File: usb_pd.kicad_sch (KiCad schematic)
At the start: 69 parts

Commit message: added digi-pote symbol, added USB_source voltage regulators
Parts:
- U?: symbol smarthome:TPS5403DR -> airsoft_controller:TPS5403DR
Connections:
- net +3V3: no longer C?.2, L?.2, U?.5 (VSENSE)
- new net +3.3V: C?.2, L?.2, U?.5 (VSENSE)
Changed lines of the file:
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@@
   (symbol (lib_id "power:GND") (at 233.68 72.39 0) (mirror y) (unit 1)
     (in_bom yes) (on_board yes) (fields_autoplaced)
-    (property "Reference" "#PWR?" (id 0) (at 233.68 78.74 0)
+    (property "Reference" "#PWR0129" (id 0) (at 233.68 78.74 0)
       (effects (font (size 1.27 1.27)) hide)
     )
@@
   (symbol (lib_id "power:GND") (at 57.15 173.99 0) (unit 1)
     (in_bom yes) (on_board yes) (fields_autoplaced)
-    (property "Reference" "#PWR?" (id 0) (at 57.15 180.34 0)
+    (property "Reference" "#PWR0147" (id 0) (at 57.15 180.34 0)
       (effects (font (size 1.27 1.27)) hide)
     )
@@
   (symbol (lib_id "power:GND") (at 96.52 106.68 0) (unit 1)
     (in_bom yes) (on_board yes) (fields_autoplaced)
-    (property "Reference" "#PWR?" (id 0) (at 96.52 113.03 0)
+    (property "Reference" "#PWR0135" (id 0) (at 96.52 113.03 0)
       (effects (font (size 1.27 1.27)) hide)
     )
@@
   (symbol (lib_id "power:GND") (at 120.65 57.15 0) (unit 1)
     (in_bom yes) (on_board yes) (fields_autoplaced)
-    (property "Reference" "#PWR?" (id 0) (at 120.65 63.5 0)
+    (property "Reference" "#PWR0137" (id 0) (at 120.65 63.5 0)
       (effects (font (size 1.27 1.27)) hide)
     )
@@
   (symbol (lib_id "power:GND") (at 168.91 128.27 0) (unit 1)
     (in_bom yes) (on_board yes) (fields_autoplaced)
-    (property "Reference" "#PWR?" (id 0) (at 168.91 134.62 0)
+    (property "Reference" "#PWR0124" (id 0) (at 168.91 134.62 0)
       (effects (font (size 1.27 1.27)) hide)
     )
@@
   (symbol (lib_id "power:+3.3V") (at 104.14 160.02 0) (unit 1)
     (in_bom yes) (on_board yes) (fields_autoplaced)
-    (property "Reference" "#PWR?" (id 0) (at 104.14 163.83 0)
+    (property "Reference" "#PWR0150" (id 0) (at 104.14 163.83 0)
       (effects (font (size 1.27 1.27)) hide)
     )
@@
   (symbol (lib_id "power:GND") (at 262.89 133.35 0) (unit 1)
     (in_bom yes) (on_board yes) (fields_autoplaced)
-    (property "Reference" "#PWR?" (id 0) (at 262.89 139.7 0)
+    (property "Reference" "#PWR0122" (id 0) (at 262.89 139.7 0)
       (effects (font (size 1.27 1.27)) hide)
     )
@@
   (symbol (lib_id "power:GND") (at 74.93 173.99 0) (unit 1)
     (in_bom yes) (on_board yes) (fields_autoplaced)
-    (property "Reference" "#PWR?" (id 0) (at 74.93 180.34 0)
+    (property "Reference" "#PWR0142" (id 0) (at 74.93 180.34 0)
       (effects (font (size 1.27 1.27)) hide)
     )
@@
   (symbol (lib_id "power:GND") (at 138.43 115.57 0) (unit 1)
     (in_bom yes) (on_board yes) (fields_autoplaced)
-    (property "Reference" "#PWR?" (id 0) (at 138.43 121.92 0)
+    (property "Reference" "#PWR0125" (id 0) (at 138.43 121.92 0)
       (effects (font (size 1.27 1.27)) hide)
     )
@@
   (symbol (lib_id "power:GND") (at 62.23 96.52 0) (unit 1)
     (in_bom yes) (on_board yes) (fields_autoplaced)
-    (property "Reference" "#PWR?" (id 0) (at 62.23 102.87 0)
+    (property "Reference" "#PWR0134" (id 0) (at 62.23 102.87 0)
       (effects (font (size 1.27 1.27)) hide)
     )
@@
   (symbol (lib_id "power:GND") (at 88.9 106.68 0) (unit 1)
     (in_bom yes) (on_board yes) (fields_autoplaced)
-    (property "Reference" "#PWR?" (id 0) (at 88.9 113.03 0)
+    (property "Reference" "#PWR0136" (id 0) (at 88.9 113.03 0)
       (effects (font (size 1.27 1.27)) hide)
     )
@@
   (symbol (lib_id "power:GND") (at 201.93 109.22 0) (unit 1)
     (in_bom yes) (on_board yes) (fields_autoplaced)
-    (property "Reference" "#PWR?" (id 0) (at 201.93 115.57 0)
+    (property "Reference" "#PWR0130" (id 0) (at 201.93 115.57 0)
       (effects (font (size 1.27 1.27)) hide)
     )
@@
   (symbol (lib_id "power:VBUS") (at 138.43 62.23 0) (unit 1)
     (in_bom yes) (on_board yes) (fields_autoplaced)
-    (property "Reference" "#PWR?" (id 0) (at 138.43 66.04 0)
+    (property "Reference" "#PWR0121" (id 0) (at 138.43 66.04 0)
       (effects (font (size 1.27 1.27)) hide)
     )
@@
   (symbol (lib_id "power:GND") (at 67.31 173.99 0) (unit 1)
     (in_bom yes) (on_board yes) (fields_autoplaced)
-    (property "Reference" "#PWR?" (id 0) (at 67.31 180.34 0)
+    (property "Reference" "#PWR0143" (id 0) (at 67.31 180.34 0)
       (effects (font (size 1.27 1.27)) hide)
     )
@@
   (symbol (lib_id "power:GND") (at 107.95 99.06 0) (unit 1)
     (in_bom yes) (on_board yes) (fields_autoplaced)
-    (property "Reference" "#PWR?" (id 0) (at 107.95 105.41 0)
+    (property "Reference" "#PWR0133" (id 0) (at 107.95 105.41 0)
       (effects (font (size 1.27 1.27)) hide)
     )
@@
   (symbol (lib_id "power:+BATT") (at 248.92 50.8 0) (unit 1)
     (in_bom yes) (on_board yes) (fields_autoplaced)
-    (property "Reference" "#PWR?" (id 0) (at 248.92 54.61 0)
+    (property "Reference" "#PWR0123" (id 0) (at 248.92 54.61 0)
       (effects (font (size 1.27 1.27)) hide)
     )
@@
   (symbol (lib_id "power:+BATT") (at 77.47 158.75 0) (unit 1)
     (in_bom yes) (on_board yes) (fields_autoplaced)
-    (property "Reference" "#PWR?" (id 0) (at 77.47 162.56 0)
+    (property "Reference" "#PWR0151" (id 0) (at 77.47 162.56 0)
       (effects (font (size 1.27 1.27)) hide)
     )
@@
   (symbol (lib_id "power:GND") (at 106.68 176.53 0) (unit 1)
     (in_bom yes) (on_board yes) (fields_autoplaced)
-    (property "Reference" "#PWR?" (id 0) (at 106.68 182.88 0)
+    (property "Reference" "#PWR0149" (id 0) (at 106.68 182.88 0)
       (effects (font (size 1.27 1.27)) hide)
     )
@@
   (symbol (lib_id "power:GND") (at 40.64 62.23 0) (unit 1)
     (in_bom yes) (on_board yes) (fields_autoplaced)
-    (property "Reference" "#PWR?" (id 0) (at 40.64 68.58 0)
+    (property "Reference" "#PWR0141" (id 0) (at 40.64 68.58 0)
       (effects (font (size 1.27 1.27)) hide)
     )
@@
   (symbol (lib_id "power:+3V3") (at 180.34 113.03 0) (unit 1)
     (in_bom yes) (on_board yes) (fields_autoplaced)
-    (property "Reference" "#PWR?" (id 0) (at 180.34 116.84 0)
+    (property "Reference" "#PWR0131" (id 0) (at 180.34 116.84 0)
       (effects (font (size 1.27 1.27)) hide)
     )
@@
     (pin "2")
   )
-  (symbol (lib_id "smarthome:TPS5403DR") (at 90.17 163.83 0) (unit 1)
+  (symbol (lib_id "airsoft_controller:TPS5403DR") (at 90.17 163.83 0) (unit 1)
     (in_bom yes) (on_board yes) (fields_autoplaced)
     (property "Reference" "U?" (id 0) (at 90.17 151.13 0))
@@
   (symbol (lib_id "power:GND") (at 71.12 72.39 0) (unit 1)
     (in_bom yes) (on_board yes) (fields_autoplaced)
-    (property "Reference" "#PWR?" (id 0) (at 71.12 78.74 0)
+    (property "Reference" "#PWR0139" (id 0) (at 71.12 78.74 0)
       (effects (font (size 1.27 1.27)) hide)
     )
@@
   (symbol (lib_id "power:+3.3V") (at 130.81 154.94 0) (unit 1)
     (in_bom yes) (on_board yes) (fields_autoplaced)
-    (property "Reference" "#PWR?" (id 0) (at 130.81 158.75 0)
+    (property "Reference" "#PWR0144" (id 0) (at 130.81 158.75 0)
       (effects (font (size 1.27 1.27)) hide)
     )
@@
   (symbol (lib_id "power:GND") (at 86.36 72.39 0) (unit 1)
     (in_bom yes) (on_board yes) (fields_autoplaced)
-    (property "Reference" "#PWR?" (id 0) (at 86.36 78.74 0)
+    (property "Reference" "#PWR0140" (id 0) (at 86.36 78.74 0)
       (effects (font (size 1.27 1.27)) hide)
     )
@@
   (symbol (lib_id "power:GND") (at 146.05 115.57 0) (unit 1)
     (in_bom yes) (on_board yes) (fields_autoplaced)
-    (property "Reference" "#PWR?" (id 0) (at 146.05 121.92 0)
+    (property "Reference" "#PWR0126" (id 0) (at 146.05 121.92 0)
       (effects (font (size 1.27 1.27)) hide)
     )
@@
   (symbol (lib_id "power:GND") (at 118.11 170.18 0) (unit 1)
     (in_bom yes) (on_board yes) (fields_autoplaced)
-    (property "Reference" "#PWR?" (id 0) (at 118.11 176.53 0)
+    (property "Reference" "#PWR0145" (id 0) (at 118.11 176.53 0)
       (effects (font (size 1.27 1.27)) hide)
     )
@@
   (symbol (lib_id "power:VBUS") (at 71.12 50.8 0) (unit 1)
     (in_bom yes) (on_board yes) (fields_autoplaced)
-    (property "Reference" "#PWR?" (id 0) (at 71.12 54.61 0)
+    (property "Reference" "#PWR0132" (id 0) (at 71.12 54.61 0)
       (effects (font (size 1.27 1.27)) hide)
     )
@@
   (symbol (lib_id "power:GND") (at 130.81 170.18 0) (unit 1)
     (in_bom yes) (on_board yes) (fields_autoplaced)
-    (property "Reference" "#PWR?" (id 0) (at 130.81 176.53 0)
+    (property "Reference" "#PWR0146" (id 0) (at 130.81 176.53 0)
       (effects (font (size 1.27 1.27)) hide)
     )
@@
   (symbol (lib_id "power:GND") (at 208.28 62.23 0) (mirror y) (unit 1)
     (in_bom yes) (on_board yes) (fields_autoplaced)
-    (property "Reference" "#PWR?" (id 0) (at 208.28 68.58 0)
+    (property "Reference" "#PWR0128" (id 0) (at 208.28 68.58 0)
       (effects (font (size 1.27 1.27)) hide)
     )
@@
   (symbol (lib_id "power:GND") (at 88.9 173.99 0) (unit 1)
     (in_bom yes) (on_board yes) (fields_autoplaced)
-    (property "Reference" "#PWR?" (id 0) (at 88.9 180.34 0)
+    (property "Reference" "#PWR0148" (id 0) (at 88.9 180.34 0)
       (effects (font (size 1.27 1.27)) hide)
     )
@@
   (symbol (lib_id "power:GND") (at 97.79 63.5 0) (unit 1)
     (in_bom yes) (on_board yes)
-    (property "Reference" "#PWR?" (id 0) (at 97.79 69.85 0)
+    (property "Reference" "#PWR0138" (id 0) (at 97.79 69.85 0)
       (effects (font (size 1.27 1.27)) hide)
     )
@@
   (symbol (lib_id "power:GND") (at 163.83 57.15 0) (mirror y) (unit 1)
     (in_bom yes) (on_board yes) (fields_autoplaced)
-    (property "Reference" "#PWR?" (id 0) (at 163.83 63.5 0)
-      (effects (font (size 1.27 1.27)) hide)
-    )
+    (property "Reference" "#PWR0127" (id 0) (at 163.83 63.5 0)
+      (effects (font (size 1.27 1.27)) hide)
+    )

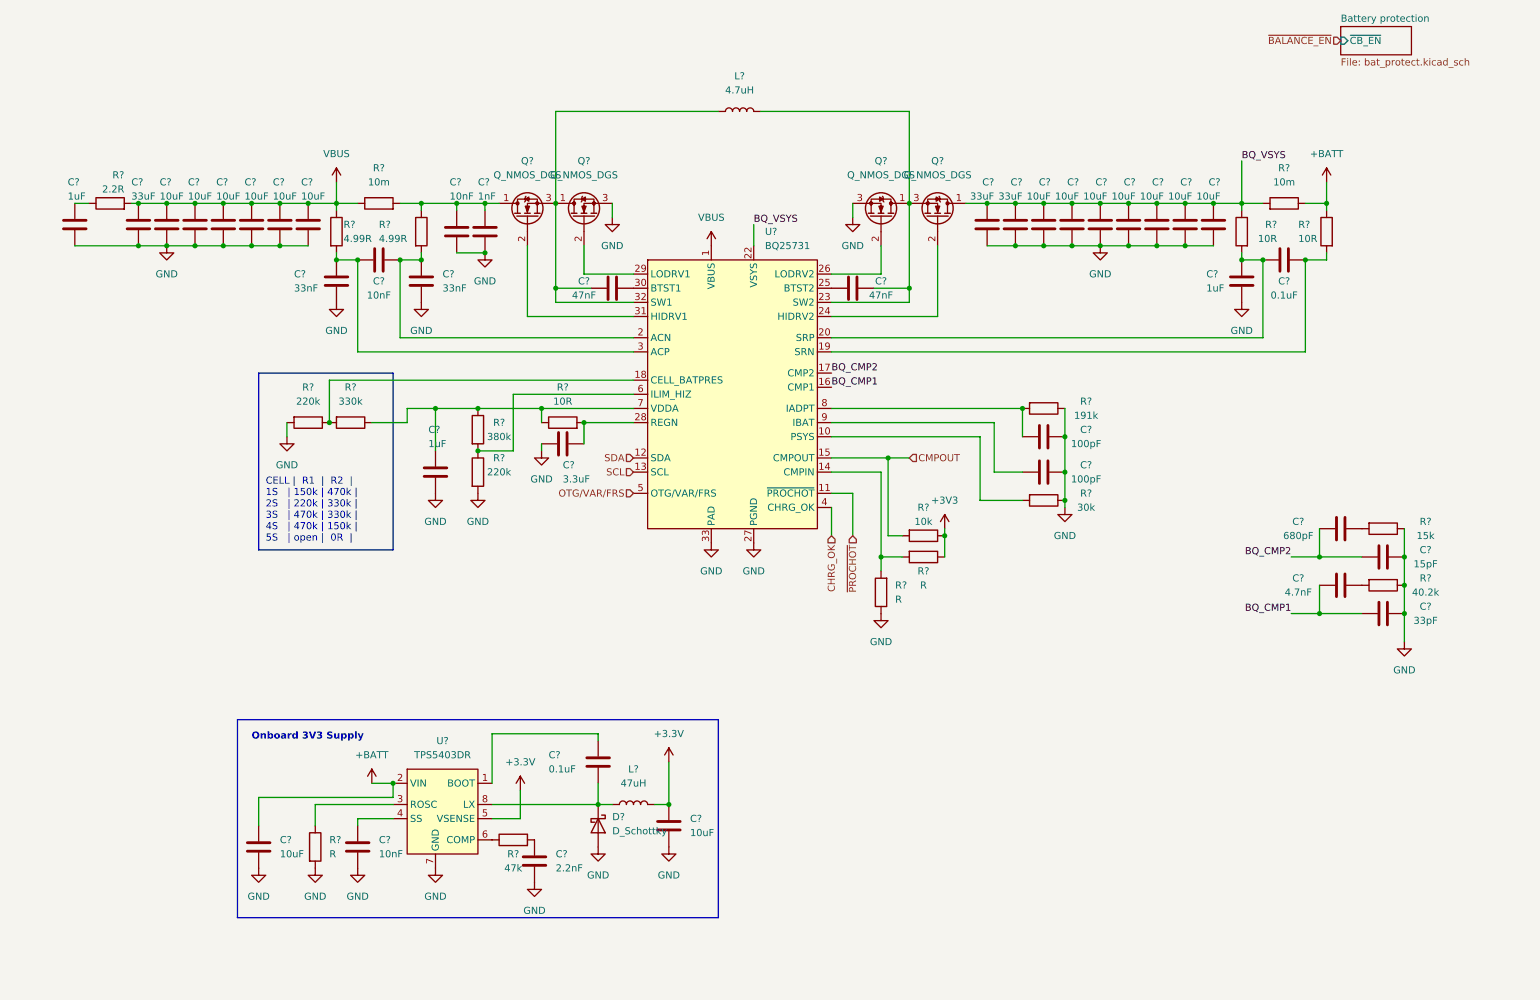
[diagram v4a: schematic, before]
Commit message: added audio ref schematic, added bat to 5V, added shift register, connected devices with other periferals
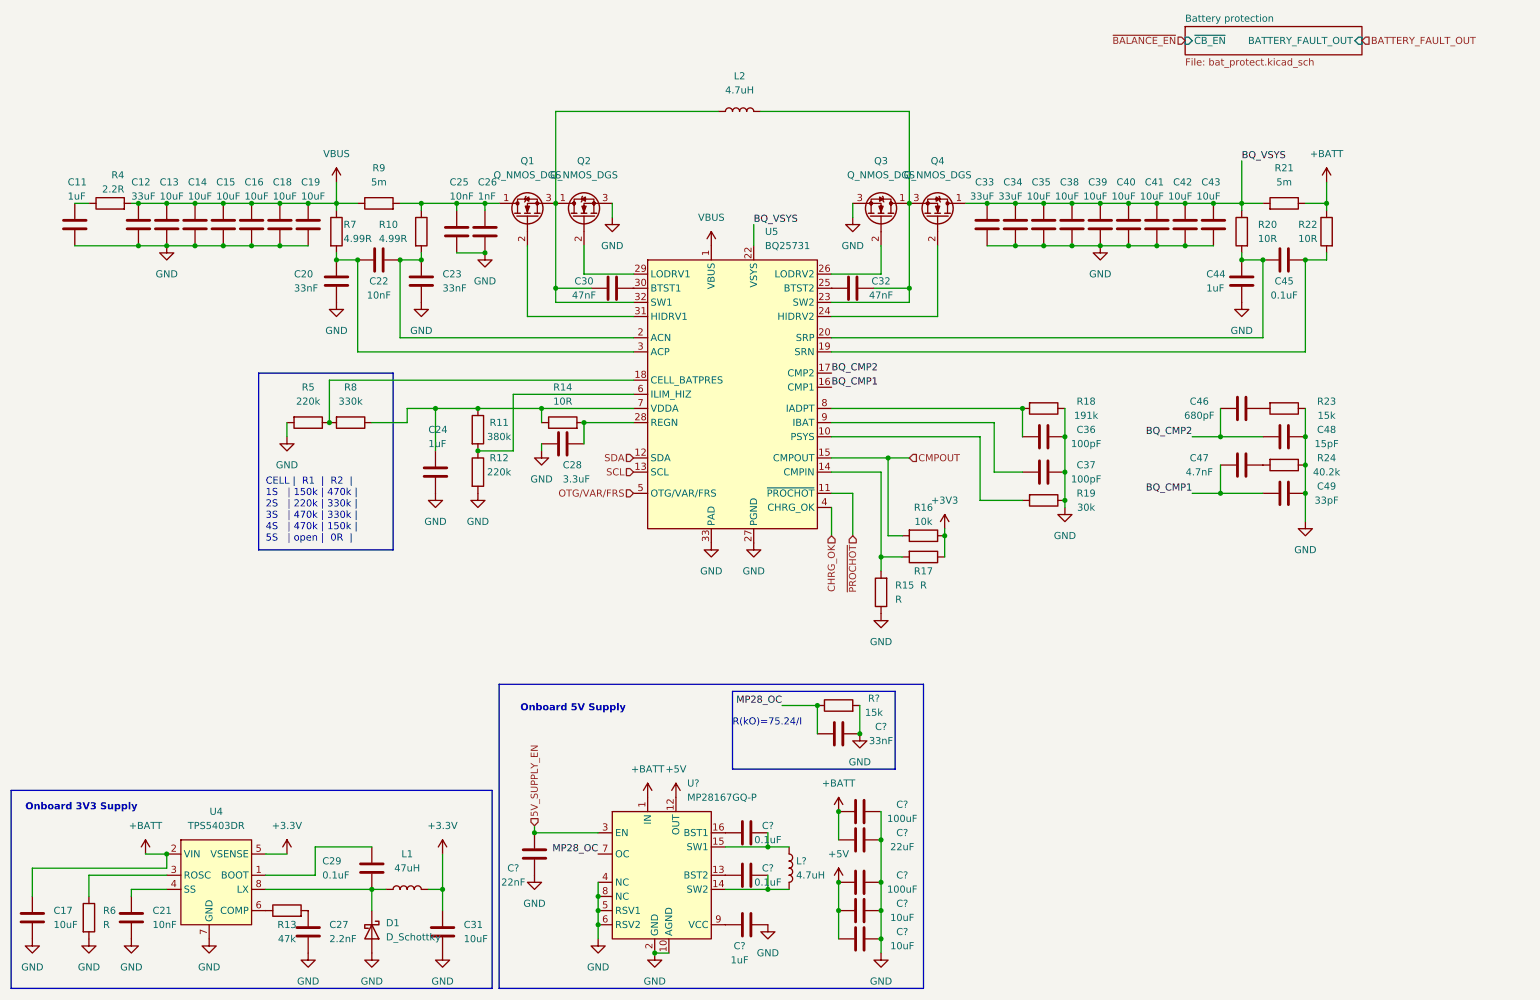
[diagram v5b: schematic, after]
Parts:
- added C? (x2): 0.1uF, symbol Device:C
- added C? (x2): 100uF, symbol Device:C
- added C?: 22nF, symbol Device:C
- added C?: 22uF, symbol Device:C
- added C?: 33nF, symbol Device:C
- added C?: 1uF, symbol Device:C
- added C? (x2): 10uF, symbol Device:C
- added L?: 4.7uH, symbol Device:L
- added R?: 15k, symbol Device:R
- added U?: MP28167GQ-P, symbol airsoft_controller:MP28167GQ-P
- R21, R9: renamed from R?; value 10m -> 5m
- gave numbers to parts that had none: 67
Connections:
- net +BATT: now also C?.1, C?.1, U?.1 (IN)
- net GND: now also C?.1, C?.2, C?.2, C?.2, C?.2, C?.2, C?.2, C?.2, R?.2, U?.10 (AGND), U?.11 (GND), U?.2 (GND), U?.4 (NC), U?.5 (RSV1), U?.6 (RSV2), U?.8 (NC)
- new net: C?.1, U?.13 (BST2)
- new net: C?.2, L?.2, U?.14 (SW2)
- new net: C?.2, L?.1, U?.15 (SW1)
- new net: C?.1, U?.16 (BST1)
- new net: C?.1, U?.9 (VCC)
- new net +5V: C?.1, C?.1, C?.1, U?.12 (OUT)
- new net 5V_SUPPLY_EN: C?.2, U?.3 (EN)
- new net MP28_OC: C?.1, R?.1, U?.7 (OC)
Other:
- sheet Battery protection ports: added BATTERY_FAULT_OUT; removed none
- note added: "Onboard 5V Supply"
- note added: "R(kO)=75.24/I"
- moved on the sheet: C17, C21, C27, C29, C31, C46, C47, C48, C49, D1, L1, R13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
